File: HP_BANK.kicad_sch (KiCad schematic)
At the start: 2 parts, among them J6 DF40HC(3.0)-120DS, J7 DF40HC(3.0)-120DS

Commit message: finishing schematic
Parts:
- removed J6, J7: DF40HC(3.0)-120DS, Connector_Hirose_DF40:Hirose_DF40C-120DS-0.4V_2x60_P0.4mm, symbol dfdtc_Connector:Conn_02x60_Odd_Even
- added J7: FX8-140P-SV1, Connector_Hirose_FX8:Hirose_FX8-140P-SV_2x70_P0.6mm, symbol dfdtc_Connector:Conn_02x70_Odd_Even
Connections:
- new net +1V2: J7.134, J7.136
- new net GND: J7.1 (Pin_1), J7.107 (Pin_107), J7.108 (Pin_108), J7.11 (Pin_11), J7.117 (Pin_117), J7.118 (Pin_118), J7.12 (Pin_12), J7.127, J7.128, J7.131, J7.132, J7.137, J7.138, J7.139, J7.140, J7.2 (Pin_2), J7.21 (Pin_21), J7.22 (Pin_22), J7.31 (Pin_31), J7.32 (Pin_32), J7.41 (Pin_41), J7.42 (Pin_42), J7.51 (Pin_51), J7.52 (Pin_52), J7.61 (Pin_61), J7.62 (Pin_62), J7.67 (Pin_67), J7.68 (Pin_68), J7.77 (Pin_77), J7.78 (Pin_78), J7.87 (Pin_87), J7.88 (Pin_88), J7.97 (Pin_97), J7.98 (Pin_98)
- new net IO_L10N_T1U_N7_QBC_AD4N_66_N: J7.50 (Pin_50)
- new net IO_L10N_T1U_N7_QBC_AD4N_67_N: J7.116 (Pin_116)
- new net IO_L10P_T1U_N6_QBC_AD4P_66_P: J7.48 (Pin_48)
- new net IO_L10P_T1U_N6_QBC_AD4P_67_P: J7.114 (Pin_114)
- new net IO_L11N_T1U_N9_GC_66_N: J7.56 (Pin_56)
- new net IO_L11N_T1U_N9_GC_67_N: J7.122
- new net IO_L11P_T1U_N8_GC_66_P: J7.54 (Pin_54)
- new net IO_L11P_T1U_N8_GC_67_P: J7.120 (Pin_120)
- new net IO_L12N_T1U_N11_GC_66_N: J7.60 (Pin_60)
- new net IO_L12N_T1U_N11_GC_67_N: J7.126
- new net IO_L12P_T1U_N10_GC_66_P: J7.58 (Pin_58)
- new net IO_L12P_T1U_N10_GC_67_P: J7.124
- new net IO_L13N_T2L_N1_GC_QBC_66_N: J7.5 (Pin_5)
- new net IO_L13N_T2L_N1_GC_QBC_67_N: J7.71 (Pin_71)
- new net IO_L13P_T2L_N0_GC_QBC_66_P: J7.3 (Pin_3)
- new net IO_L13P_T2L_N0_GC_QBC_67_P: J7.69 (Pin_69)
- new net IO_L14N_T2L_N3_GC_66_N: J7.9 (Pin_9)
- new net IO_L14N_T2L_N3_GC_67_N: J7.75 (Pin_75)
- new net IO_L14P_T2L_N2_GC_66_P: J7.7 (Pin_7)
- new net IO_L14P_T2L_N2_GC_67_P: J7.73 (Pin_73)
- new net IO_L15N_T2L_N5_AD11N_66_N: J7.15 (Pin_15)
- new net IO_L15N_T2L_N5_AD11N_67_N: J7.81 (Pin_81)
- new net IO_L15P_T2L_N4_AD11P_66_P: J7.13 (Pin_13)
- new net IO_L15P_T2L_N4_AD11P_67_P: J7.79 (Pin_79)
- new net IO_L16N_T2U_N7_QBC_AD3N_66_N: J7.19 (Pin_19)
- new net IO_L16N_T2U_N7_QBC_AD3N_67_N: J7.85 (Pin_85)
- new net IO_L16P_T2U_N6_QBC_AD3P_66_P: J7.17 (Pin_17)
- new net IO_L16P_T2U_N6_QBC_AD3P_67_P: J7.83 (Pin_83)
- new net IO_L17N_T2U_N9_AD10N_66_N: J7.25 (Pin_25)
- new net IO_L17N_T2U_N9_AD10N_67_N: J7.91 (Pin_91)
- new net IO_L17P_T2U_N8_AD10P_66_P: J7.23 (Pin_23)
- new net IO_L17P_T2U_N8_AD10P_67_P: J7.89 (Pin_89)
- new net IO_L18N_T2U_N11_AD2N_66_N: J7.29 (Pin_29)
- new net IO_L18N_T2U_N11_AD2N_67_N: J7.95 (Pin_95)
- new net IO_L18P_T2U_N10_AD2P_66_P: J7.27 (Pin_27)
- new net IO_L18P_T2U_N10_AD2P_67_P: J7.93 (Pin_93)
- new net IO_L19N_T3L_N1_DBC_AD9N_66_N: J7.35 (Pin_35)
- new net IO_L19N_T3L_N1_DBC_AD9N_67_N: J7.101 (Pin_101)
- new net IO_L19P_T3L_N0_DBC_AD9P_66_P: J7.33 (Pin_33)
- new net IO_L19P_T3L_N0_DBC_AD9P_67_P: J7.99 (Pin_99)
- new net IO_L1N_T0L_N1_DBC_66_N: J7.6 (Pin_6)
- new net IO_L1N_T0L_N1_DBC_67_N: J7.72 (Pin_72)
- new net IO_L1P_T0L_N0_DBC_66_P: J7.4 (Pin_4)
- new net IO_L1P_T0L_N0_DBC_67_P: J7.70 (Pin_70)
- new net IO_L20N_T3L_N3_AD1N_66_N: J7.39 (Pin_39)
- new net IO_L20N_T3L_N3_AD1N_67_N: J7.105 (Pin_105)
- new net IO_L20P_T3L_N2_AD1P_66_P: J7.37 (Pin_37)
- new net IO_L20P_T3L_N2_AD1P_67_P: J7.103 (Pin_103)
- new net IO_L21N_T3L_N5_AD8N_66_N: J7.45 (Pin_45)
- new net IO_L21N_T3L_N5_AD8N_67_N: J7.111 (Pin_111)
- new net IO_L21P_T3L_N4_AD8P_66_P: J7.43 (Pin_43)
- new net IO_L21P_T3L_N4_AD8P_67_P: J7.109 (Pin_109)
- new net IO_L22N_T3U_N7_DBC_AD0N_66_N: J7.49 (Pin_49)
- new net IO_L22N_T3U_N7_DBC_AD0N_67_N: J7.115 (Pin_115)
- new net IO_L22P_T3U_N6_DBC_AD0P_66_P: J7.47 (Pin_47)
- new net IO_L22P_T3U_N6_DBC_AD0P_67_P: J7.113 (Pin_113)
- new net IO_L23N_T3U_N9_66_N: J7.55 (Pin_55)
- new net IO_L23N_T3U_N9_67_N: J7.121
- new net IO_L23P_T3U_N8_66_P: J7.53 (Pin_53)
- new net IO_L23P_T3U_N8_67_P: J7.119 (Pin_119)
- new net IO_L24N_T3U_N11_66_N: J7.59 (Pin_59)
- new net IO_L24N_T3U_N11_67_N: J7.125
- new net IO_L24P_T3U_N10_66_P: J7.57 (Pin_57)
- new net IO_L24P_T3U_N10_67_P: J7.123
- new net IO_L2N_T0L_N3_66_N: J7.10 (Pin_10)
- new net IO_L2N_T0L_N3_67_N: J7.76 (Pin_76)
- new net IO_L2P_T0L_N2_66_P: J7.8 (Pin_8)
- new net IO_L2P_T0L_N2_67_P: J7.74 (Pin_74)
- new net IO_L3N_T0L_N5_AD15N_66_N: J7.16 (Pin_16)
- new net IO_L3N_T0L_N5_AD15N_67_N: J7.82 (Pin_82)
- new net IO_L3P_T0L_N4_AD15P_66_P: J7.14 (Pin_14)
- new net IO_L3P_T0L_N4_AD15P_67_P: J7.80 (Pin_80)
- new net IO_L4N_T0U_N7_DBC_AD7N_66_N: J7.20 (Pin_20)
- new net IO_L4N_T0U_N7_DBC_AD7N_67_N: J7.86 (Pin_86)
- new net IO_L4P_T0U_N6_DBC_AD7P_66_P: J7.18 (Pin_18)
- new net IO_L4P_T0U_N6_DBC_AD7P_67_P: J7.84 (Pin_84)
- new net IO_L5N_T0U_N9_AD14N_66_N: J7.26 (Pin_26)
- new net IO_L5N_T0U_N9_AD14N_67_N: J7.92 (Pin_92)
- new net IO_L5P_T0U_N8_AD14P_66_P: J7.24 (Pin_24)
- new net IO_L5P_T0U_N8_AD14P_67_P: J7.90 (Pin_90)
- new net IO_L6N_T0U_N11_AD6N_66_N: J7.30 (Pin_30)
- new net IO_L6N_T0U_N11_AD6N_67_N: J7.96 (Pin_96)
- new net IO_L6P_T0U_N10_AD6P_66_P: J7.28 (Pin_28)
- new net IO_L6P_T0U_N10_AD6P_67_P: J7.94 (Pin_94)
- new net IO_L7N_T1L_N1_QBC_AD13N_66_N: J7.36 (Pin_36)
- new net IO_L7N_T1L_N1_QBC_AD13N_67_N: J7.102 (Pin_102)
- new net IO_L7P_T1L_N0_QBC_AD13P_66_P: J7.34 (Pin_34)
- new net IO_L7P_T1L_N0_QBC_AD13P_67_P: J7.100 (Pin_100)
- new net IO_L8N_T1L_N3_AD5N_66_N: J7.40 (Pin_40)
- new net IO_L8N_T1L_N3_AD5N_67_N: J7.106 (Pin_106)
- new net IO_L8P_T1L_N2_AD5P_66_P: J7.38 (Pin_38)
- new net IO_L8P_T1L_N2_AD5P_67_P: J7.104 (Pin_104)
- new net IO_L9N_T1L_N5_AD12N_66_N: J7.46 (Pin_46)
- new net IO_L9N_T1L_N5_AD12N_67_N: J7.112 (Pin_112)
- new net IO_L9P_T1L_N4_AD12P_66_P: J7.44 (Pin_44)
- new net IO_L9P_T1L_N4_AD12P_67_P: J7.110 (Pin_110)
- new net IO_T1U_N12_66: J7.64 (Pin_64)
- new net IO_T1U_N12_67: J7.65 (Pin_65)
- new net IO_T2U_N12_66: J7.66 (Pin_66)
- new net IO_T2U_N12_67: J7.130
- new net IO_T3U_N12_66: J7.63 (Pin_63)
- new net IO_T3U_N12_67: J7.129
- new net VCCO_HP: J7.133, J7.135

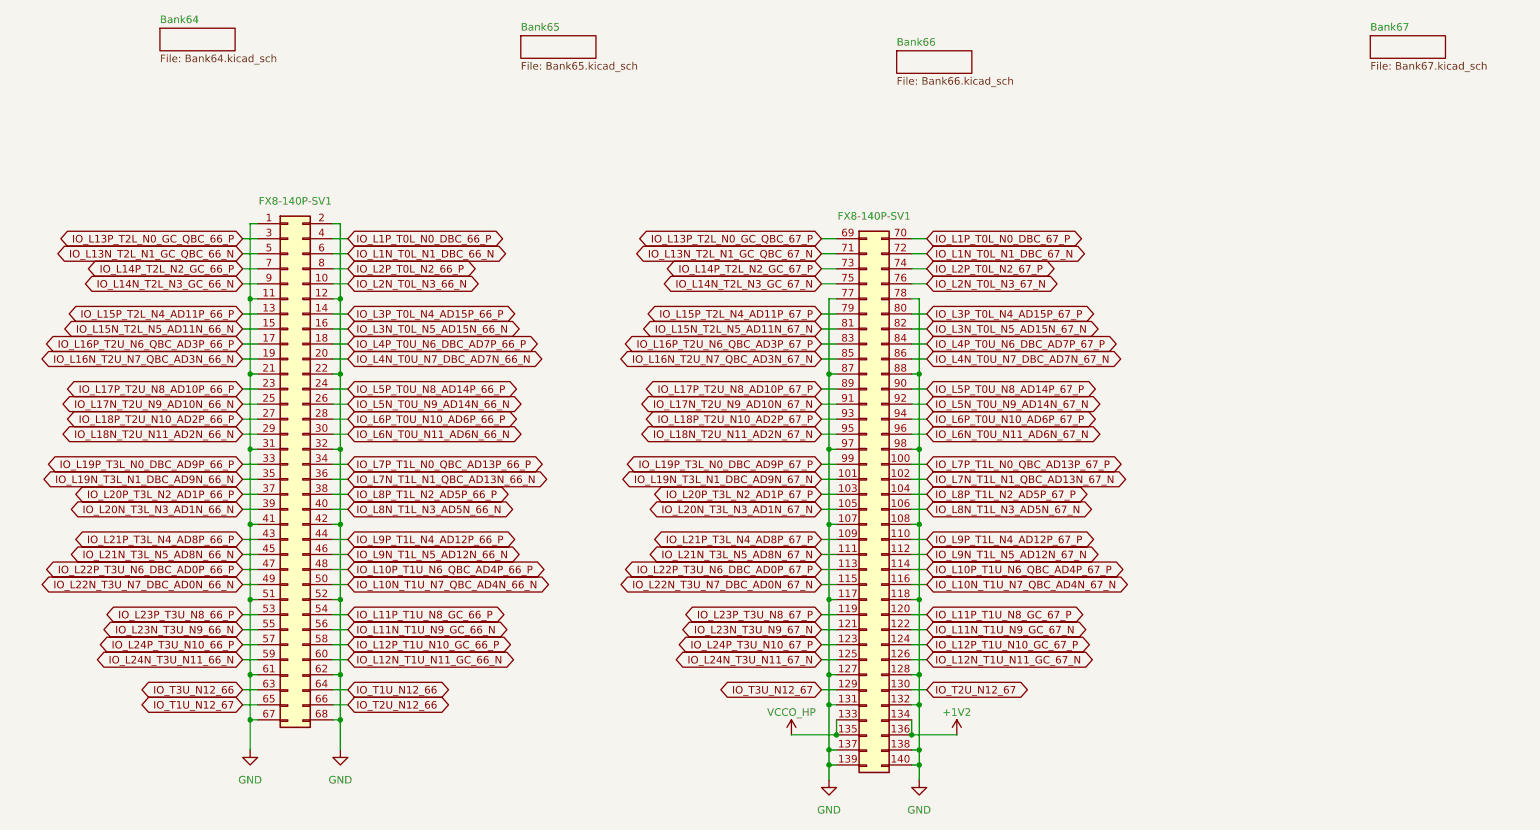
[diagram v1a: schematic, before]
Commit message: change net name to of IO diff pairs, add a scripts for name modification
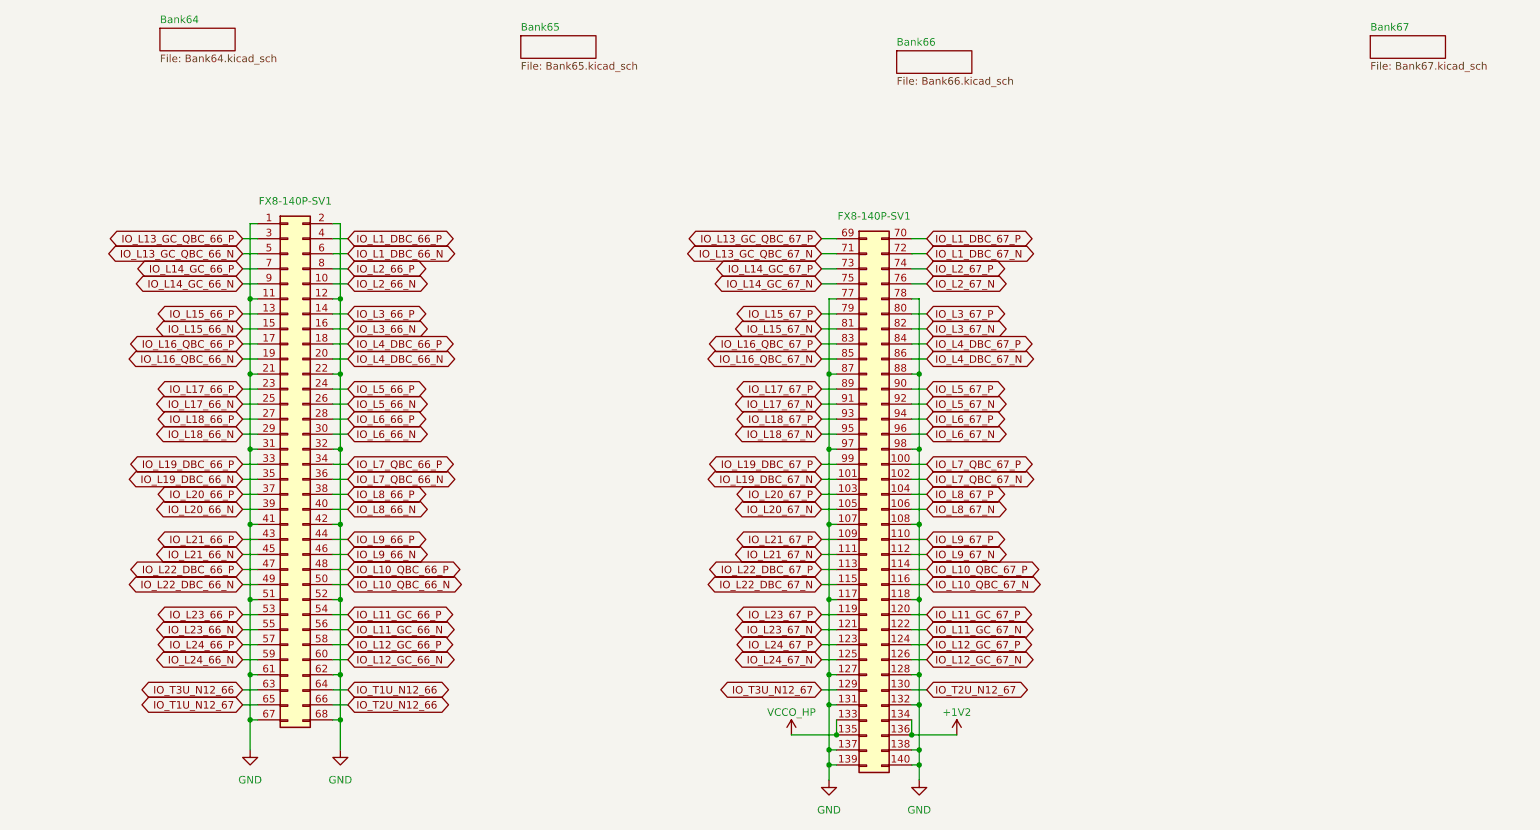
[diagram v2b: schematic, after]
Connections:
- net IO_L10N_T1U_N7_QBC_AD4N_66_N renamed IO_L10_QBC_66_N
- net IO_L10N_T1U_N7_QBC_AD4N_67_N renamed IO_L10_QBC_67_N
- net IO_L10P_T1U_N6_QBC_AD4P_66_P renamed IO_L10_QBC_66_P
- net IO_L10P_T1U_N6_QBC_AD4P_67_P renamed IO_L10_QBC_67_P
- net IO_L11N_T1U_N9_GC_66_N renamed IO_L11_GC_66_N
- net IO_L11N_T1U_N9_GC_67_N renamed IO_L11_GC_67_N
- net IO_L11P_T1U_N8_GC_66_P renamed IO_L11_GC_66_P
- net IO_L11P_T1U_N8_GC_67_P renamed IO_L11_GC_67_P
- net IO_L12N_T1U_N11_GC_66_N renamed IO_L12_GC_66_N
- net IO_L12N_T1U_N11_GC_67_N renamed IO_L12_GC_67_N
- net IO_L12P_T1U_N10_GC_66_P renamed IO_L12_GC_66_P
- net IO_L12P_T1U_N10_GC_67_P renamed IO_L12_GC_67_P
- net IO_L13N_T2L_N1_GC_QBC_66_N renamed IO_L13_GC_QBC_66_N
- net IO_L13N_T2L_N1_GC_QBC_67_N renamed IO_L13_GC_QBC_67_N
- net IO_L13P_T2L_N0_GC_QBC_66_P renamed IO_L13_GC_QBC_66_P
- net IO_L13P_T2L_N0_GC_QBC_67_P renamed IO_L13_GC_QBC_67_P
- net IO_L14N_T2L_N3_GC_66_N renamed IO_L14_GC_66_N
- net IO_L14N_T2L_N3_GC_67_N renamed IO_L14_GC_67_N
- net IO_L14P_T2L_N2_GC_66_P renamed IO_L14_GC_66_P
- net IO_L14P_T2L_N2_GC_67_P renamed IO_L14_GC_67_P
- net IO_L15N_T2L_N5_AD11N_66_N renamed IO_L15_66_N
- net IO_L15N_T2L_N5_AD11N_67_N renamed IO_L15_67_N
- net IO_L15P_T2L_N4_AD11P_66_P renamed IO_L15_66_P
- net IO_L15P_T2L_N4_AD11P_67_P renamed IO_L15_67_P
- net IO_L16N_T2U_N7_QBC_AD3N_66_N renamed IO_L16_QBC_66_N
- net IO_L16N_T2U_N7_QBC_AD3N_67_N renamed IO_L16_QBC_67_N
- net IO_L16P_T2U_N6_QBC_AD3P_66_P renamed IO_L16_QBC_66_P
- net IO_L16P_T2U_N6_QBC_AD3P_67_P renamed IO_L16_QBC_67_P
- net IO_L17N_T2U_N9_AD10N_66_N renamed IO_L17_66_N
- net IO_L17N_T2U_N9_AD10N_67_N renamed IO_L17_67_N
- net IO_L17P_T2U_N8_AD10P_66_P renamed IO_L17_66_P
- net IO_L17P_T2U_N8_AD10P_67_P renamed IO_L17_67_P
- net IO_L18N_T2U_N11_AD2N_66_N renamed IO_L18_66_N
- net IO_L18N_T2U_N11_AD2N_67_N renamed IO_L18_67_N
- net IO_L18P_T2U_N10_AD2P_66_P renamed IO_L18_66_P
- net IO_L18P_T2U_N10_AD2P_67_P renamed IO_L18_67_P
- net IO_L19N_T3L_N1_DBC_AD9N_66_N renamed IO_L19_DBC_66_N
- net IO_L19N_T3L_N1_DBC_AD9N_67_N renamed IO_L19_DBC_67_N
- net IO_L19P_T3L_N0_DBC_AD9P_66_P renamed IO_L19_DBC_66_P
- net IO_L19P_T3L_N0_DBC_AD9P_67_P renamed IO_L19_DBC_67_P
- net IO_L1N_T0L_N1_DBC_66_N renamed IO_L1_DBC_66_N
- net IO_L1N_T0L_N1_DBC_67_N renamed IO_L1_DBC_67_N
- net IO_L1P_T0L_N0_DBC_66_P renamed IO_L1_DBC_66_P
- net IO_L1P_T0L_N0_DBC_67_P renamed IO_L1_DBC_67_P
- net IO_L20N_T3L_N3_AD1N_66_N renamed IO_L20_66_N
- net IO_L20N_T3L_N3_AD1N_67_N renamed IO_L20_67_N
- net IO_L20P_T3L_N2_AD1P_66_P renamed IO_L20_66_P
- net IO_L20P_T3L_N2_AD1P_67_P renamed IO_L20_67_P
- net IO_L21N_T3L_N5_AD8N_66_N renamed IO_L21_66_N
- net IO_L21N_T3L_N5_AD8N_67_N renamed IO_L21_67_N
- net IO_L21P_T3L_N4_AD8P_66_P renamed IO_L21_66_P
- net IO_L21P_T3L_N4_AD8P_67_P renamed IO_L21_67_P
- net IO_L22N_T3U_N7_DBC_AD0N_66_N renamed IO_L22_DBC_66_N
- net IO_L22N_T3U_N7_DBC_AD0N_67_N renamed IO_L22_DBC_67_N
- net IO_L22P_T3U_N6_DBC_AD0P_66_P renamed IO_L22_DBC_66_P
- net IO_L22P_T3U_N6_DBC_AD0P_67_P renamed IO_L22_DBC_67_P
- net IO_L23N_T3U_N9_66_N renamed IO_L23_66_N
- net IO_L23N_T3U_N9_67_N renamed IO_L23_67_N
- net IO_L23P_T3U_N8_66_P renamed IO_L23_66_P
- net IO_L23P_T3U_N8_67_P renamed IO_L23_67_P
- net IO_L24N_T3U_N11_66_N renamed IO_L24_66_N
- net IO_L24N_T3U_N11_67_N renamed IO_L24_67_N
- net IO_L24P_T3U_N10_66_P renamed IO_L24_66_P
- net IO_L24P_T3U_N10_67_P renamed IO_L24_67_P
- net IO_L2N_T0L_N3_66_N renamed IO_L2_66_N
- net IO_L2N_T0L_N3_67_N renamed IO_L2_67_N
- net IO_L2P_T0L_N2_66_P renamed IO_L2_66_P
- net IO_L2P_T0L_N2_67_P renamed IO_L2_67_P
- net IO_L3N_T0L_N5_AD15N_66_N renamed IO_L3_66_N
- net IO_L3N_T0L_N5_AD15N_67_N renamed IO_L3_67_N
- net IO_L3P_T0L_N4_AD15P_66_P renamed IO_L3_66_P
- net IO_L3P_T0L_N4_AD15P_67_P renamed IO_L3_67_P
- net IO_L4N_T0U_N7_DBC_AD7N_66_N renamed IO_L4_DBC_66_N
- net IO_L4N_T0U_N7_DBC_AD7N_67_N renamed IO_L4_DBC_67_N
- net IO_L4P_T0U_N6_DBC_AD7P_66_P renamed IO_L4_DBC_66_P
- net IO_L4P_T0U_N6_DBC_AD7P_67_P renamed IO_L4_DBC_67_P
- net IO_L5N_T0U_N9_AD14N_66_N renamed IO_L5_66_N
- net IO_L5N_T0U_N9_AD14N_67_N renamed IO_L5_67_N
- net IO_L5P_T0U_N8_AD14P_66_P renamed IO_L5_66_P
- net IO_L5P_T0U_N8_AD14P_67_P renamed IO_L5_67_P
- net IO_L6N_T0U_N11_AD6N_66_N renamed IO_L6_66_N
- net IO_L6N_T0U_N11_AD6N_67_N renamed IO_L6_67_N
- net IO_L6P_T0U_N10_AD6P_66_P renamed IO_L6_66_P
- net IO_L6P_T0U_N10_AD6P_67_P renamed IO_L6_67_P
- net IO_L7N_T1L_N1_QBC_AD13N_66_N renamed IO_L7_QBC_66_N
- net IO_L7N_T1L_N1_QBC_AD13N_67_N renamed IO_L7_QBC_67_N
- net IO_L7P_T1L_N0_QBC_AD13P_66_P renamed IO_L7_QBC_66_P
- net IO_L7P_T1L_N0_QBC_AD13P_67_P renamed IO_L7_QBC_67_P
- net IO_L8N_T1L_N3_AD5N_66_N renamed IO_L8_66_N
- net IO_L8N_T1L_N3_AD5N_67_N renamed IO_L8_67_N
- net IO_L8P_T1L_N2_AD5P_66_P renamed IO_L8_66_P
- net IO_L8P_T1L_N2_AD5P_67_P renamed IO_L8_67_P
- net IO_L9N_T1L_N5_AD12N_66_N renamed IO_L9_66_N
- net IO_L9N_T1L_N5_AD12N_67_N renamed IO_L9_67_N
- net IO_L9P_T1L_N4_AD12P_66_P renamed IO_L9_66_P
- net IO_L9P_T1L_N4_AD12P_67_P renamed IO_L9_67_P
